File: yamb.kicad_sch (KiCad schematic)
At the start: 14 parts, among them J1 Barrel_Jack, J2 I2C, J3 HEADER, J4 HEADER_2.54, J5 Remote_Reset, J6 Power_Switch, P1 USB_C_Plug_USB2.0, SW1 RESET, U1 TPS3808DBV, U2 MCSBC, U3 SVR, U4 RAK4630

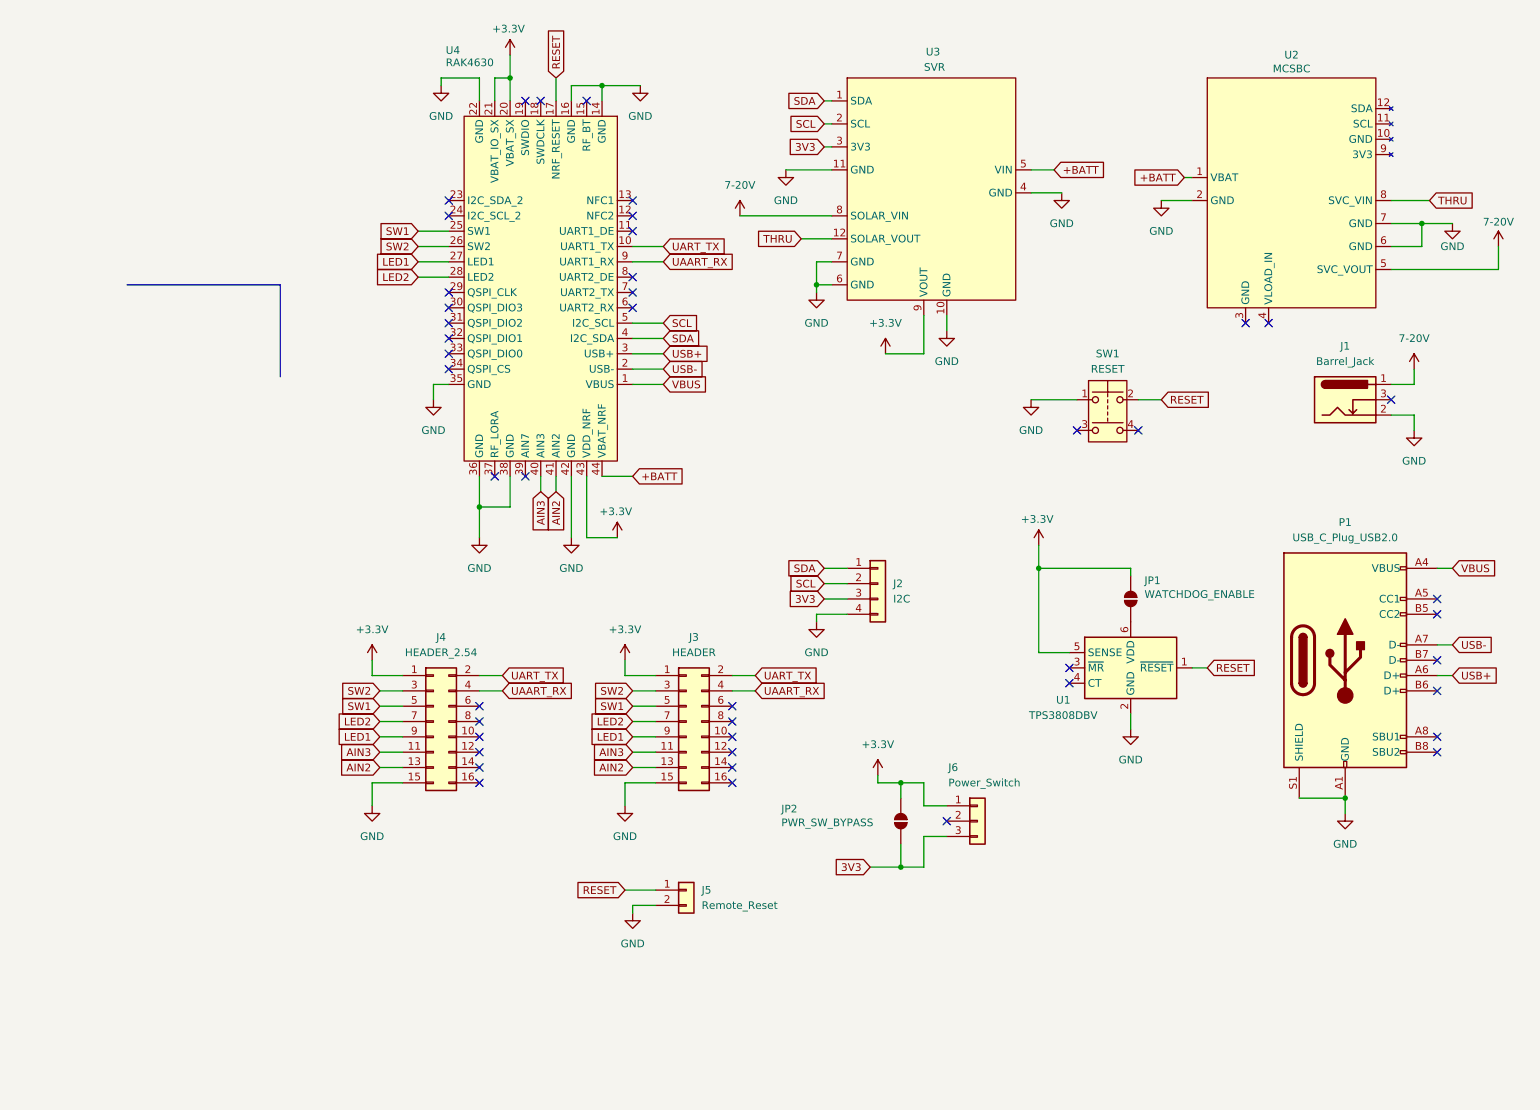
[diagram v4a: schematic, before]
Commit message: solving ERC errors
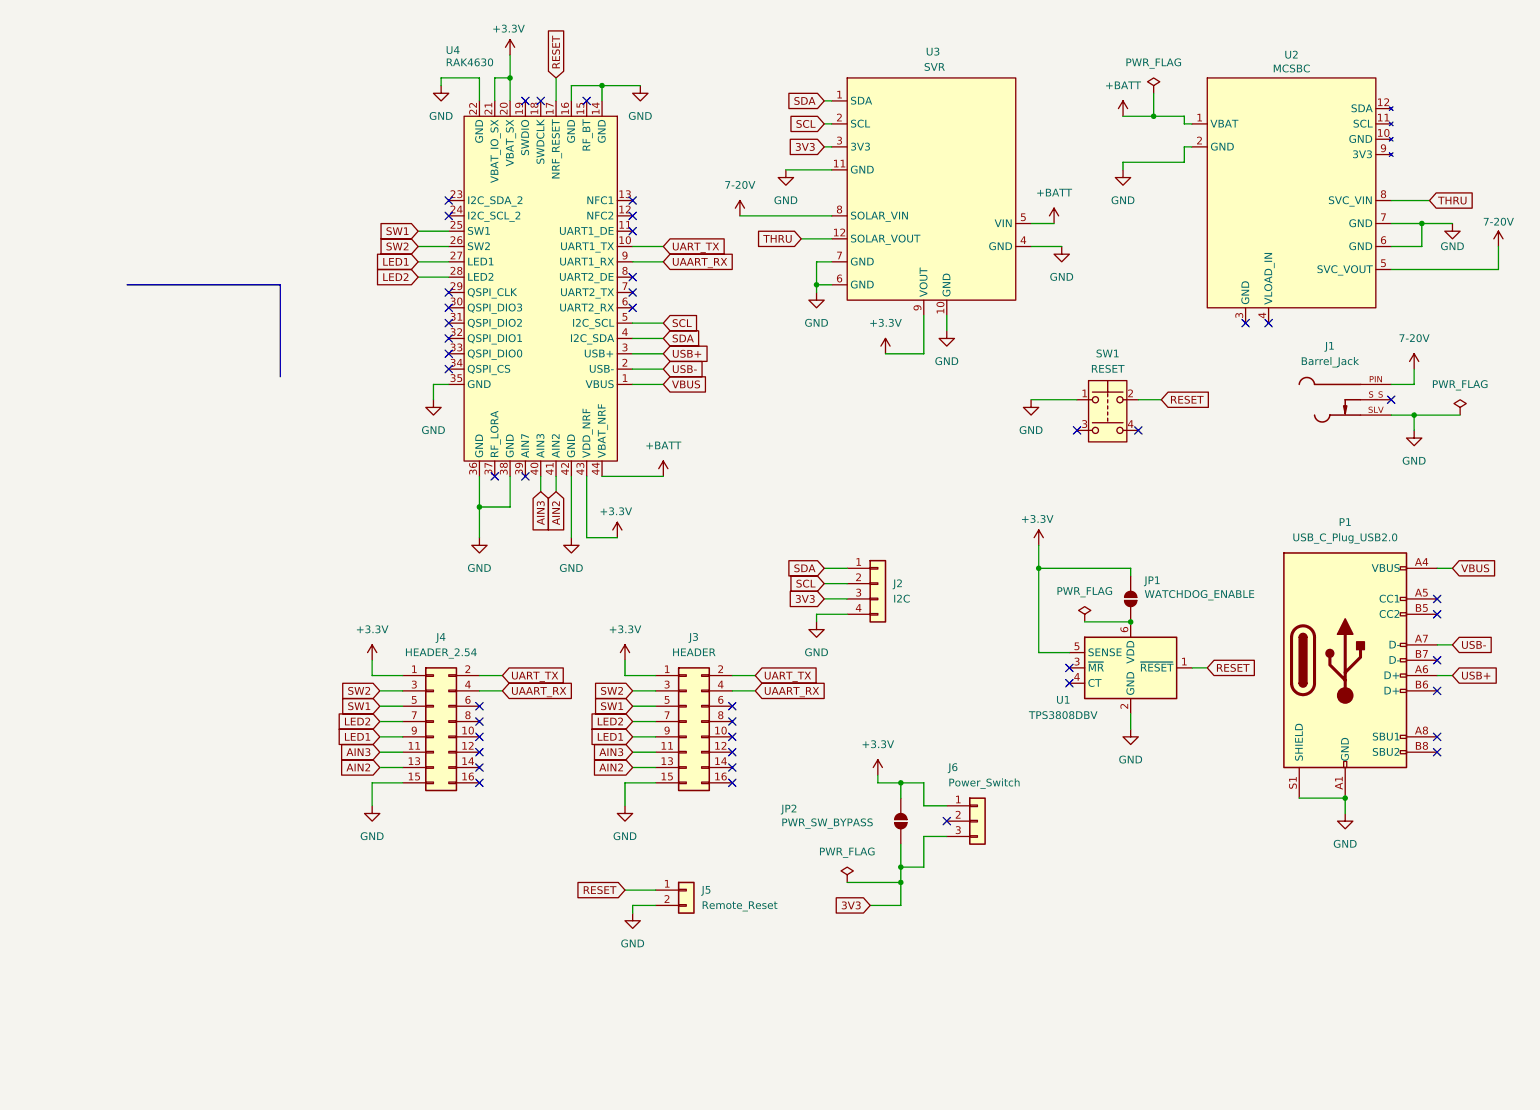
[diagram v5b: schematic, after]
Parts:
- J1: symbol Connector:Barrel_Jack_Switch -> Connector:PC722A; MANUFACTURER (none) -> Switchcraft; MAXIMUM_PACKAGE_HEIGHT (none) -> 16.764 mm; PARTREV (none) -> G; STANDARD (none) -> Manufacturer Recommendations
- U2: footprint Converter_DCDC:Voltaic_MCSBC -> Andy_Footprints:Voltaic_MCSBC
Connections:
- net 7-20V: now also J1.PIN; no longer J1.1
- net GND: now also J1.SLV; no longer J1.2

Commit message: PCB layout first pass
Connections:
- net LED1: now also J3.5 (Pin_5), J4.5 (Pin_5); no longer J3.9 (Pin_9), J4.9 (Pin_9)
- net LED2: now also J3.3 (Pin_3), J4.3 (Pin_3); no longer J3.7 (Pin_7), J4.7 (Pin_7)
- net SW1: now also J3.9 (Pin_9), J4.9 (Pin_9); no longer J3.5 (Pin_5), J4.5 (Pin_5)
- net SW2: now also J3.7 (Pin_7), J4.7 (Pin_7); no longer J3.3 (Pin_3), J4.3 (Pin_3)

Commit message: some board layout stuff
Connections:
- net +3.3V: no longer J3.1 (Pin_1), J4.1 (Pin_1), JP1.1 (A), U1.5 (SENSE), U4.20 (VBAT_SX), U4.21 (VBAT_IO_SX), U4.43 (VDD_NRF)
- net 3V3: now also J3.1 (Pin_1), J4.1 (Pin_1), JP1.1 (A), U1.5 (SENSE), U4.20 (VBAT_SX), U4.21 (VBAT_IO_SX), U4.43 (VDD_NRF)

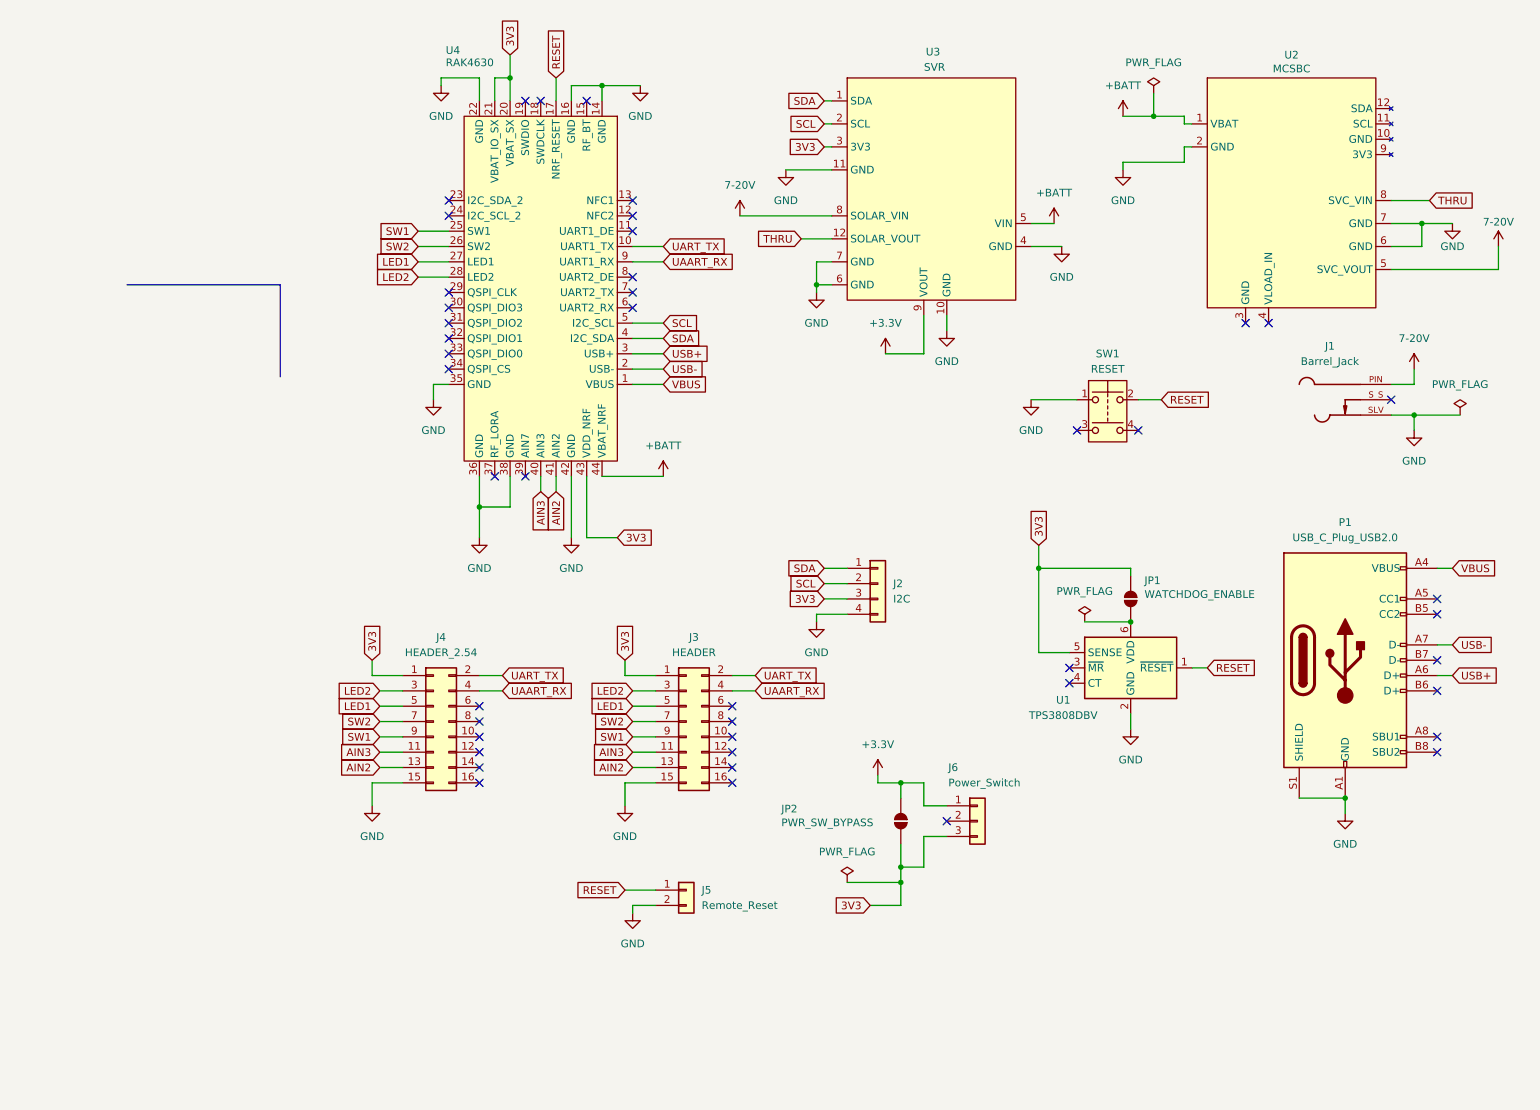
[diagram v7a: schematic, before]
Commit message: some 3D components, adding BME280, some 3V3 vs 3.3V fixes
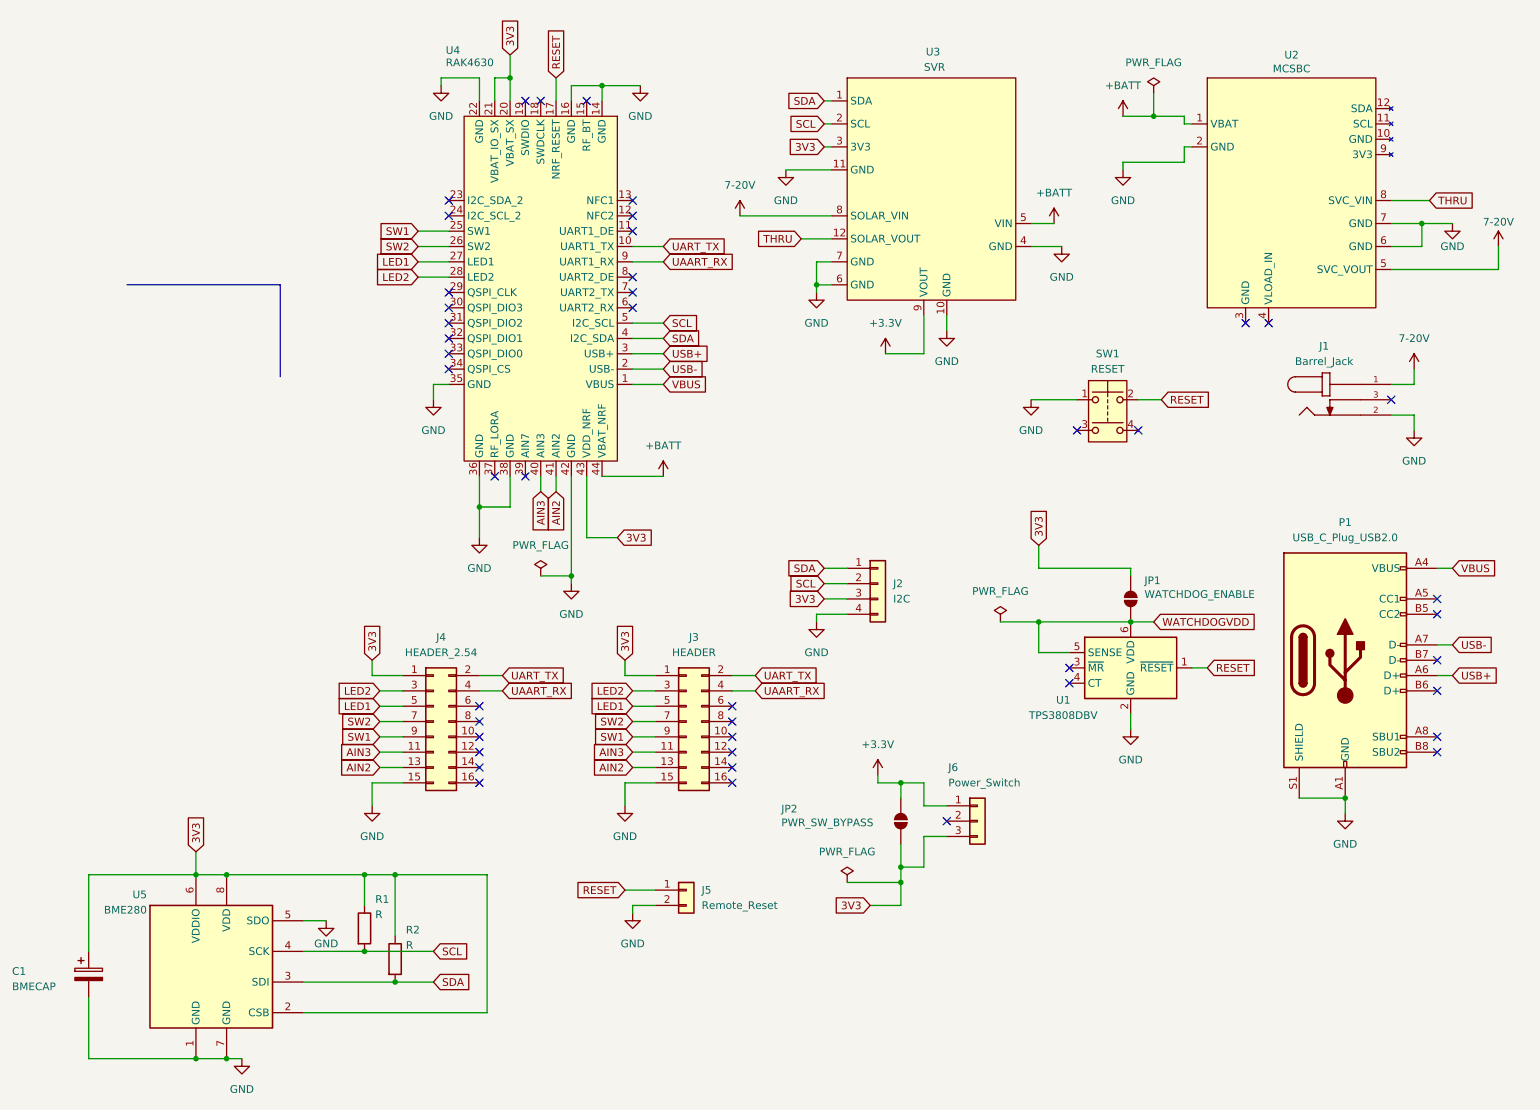
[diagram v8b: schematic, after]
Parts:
- added C1: BMECAP, Capacitor_SMD:C_1206_3216Metric_Pad1.33x1.80mm_HandSolder, symbol Device:C_Polarized
- added R1, R2: R, Resistor_SMD:R_1206_3216Metric_Pad1.30x1.75mm_HandSolder, symbol Device:R
- added U5: BME280, Package_LGA:Bosch_LGA-8_2.5x2.5mm_P0.65mm_ClockwisePinNumbering, symbol Sensor:BME280
- J1: footprint Connector_BarrelJack:SWITCHCRAFT_PC722A -> Andy_Footprints:CUI_PJ-044A; symbol Connector:PC722A -> Andy_Symbols:PJ-044A; MANUFACTURER Switchcraft -> CUI; PARTREV G -> 1.02
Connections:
- net 3V3: now also C1.1, R1.1, R2.1, U5.2 (CSB), U5.6 (VDDIO), U5.8 (VDD); no longer U1.5 (SENSE)
- net 7-20V: now also J1.1; no longer J1.PIN
- net GND: now also J1.2, C1.2, U5.1 (GND), U5.5 (SDO), U5.7 (GND); no longer J1.SLV
- net SCL: now also R1.2, U5.4 (SCK)
- net SDA: now also R2.2, U5.3 (SDI)
- net WATCHDOGVDD: now reaches JP1.2 (B), U1.6 (VDD)
- net WATCHDOGVDD: now also U1.5 (SENSE)
